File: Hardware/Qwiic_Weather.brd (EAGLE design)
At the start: 25.4 x 25.4 mm, 22 parts, among them J1 Qwiic Right Angle, J3 Qwiic Right Angle, J4 PTH, U3 BME280

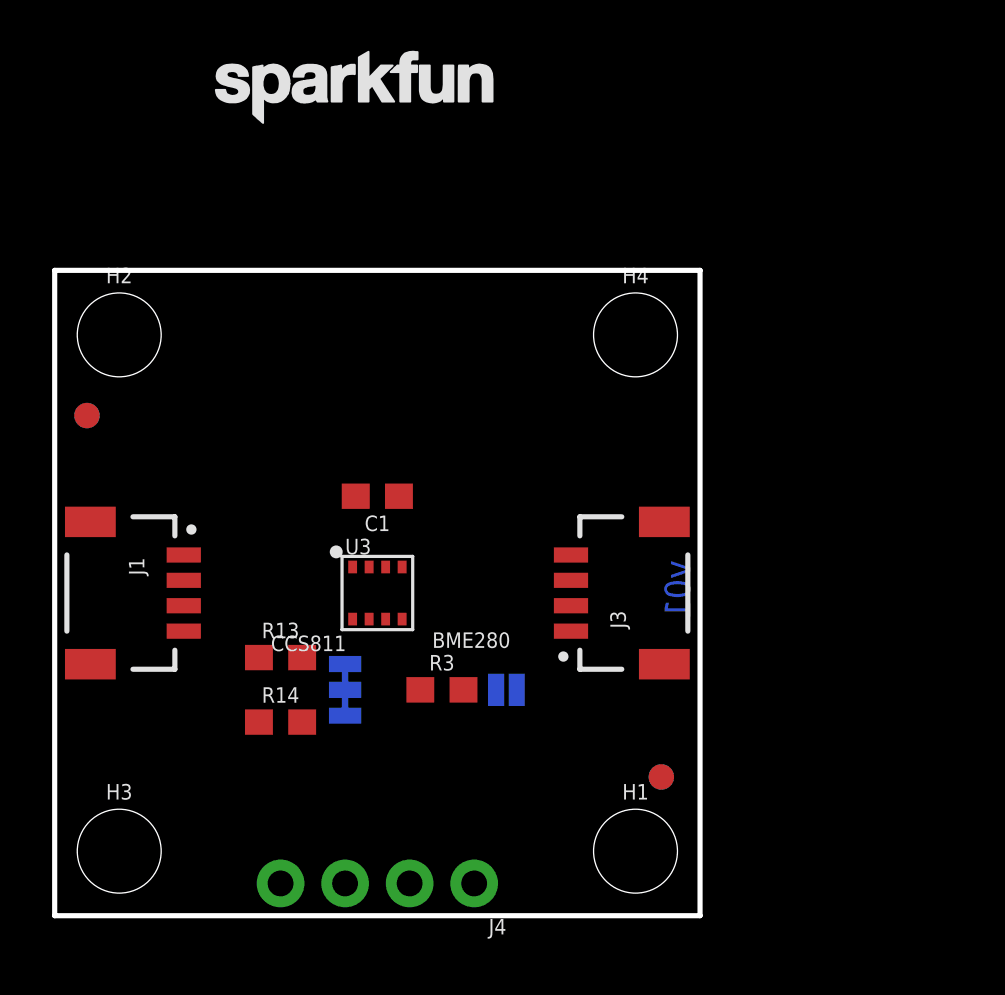
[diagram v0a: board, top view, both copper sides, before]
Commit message: added SPI cabability and some prelim buzzard label work
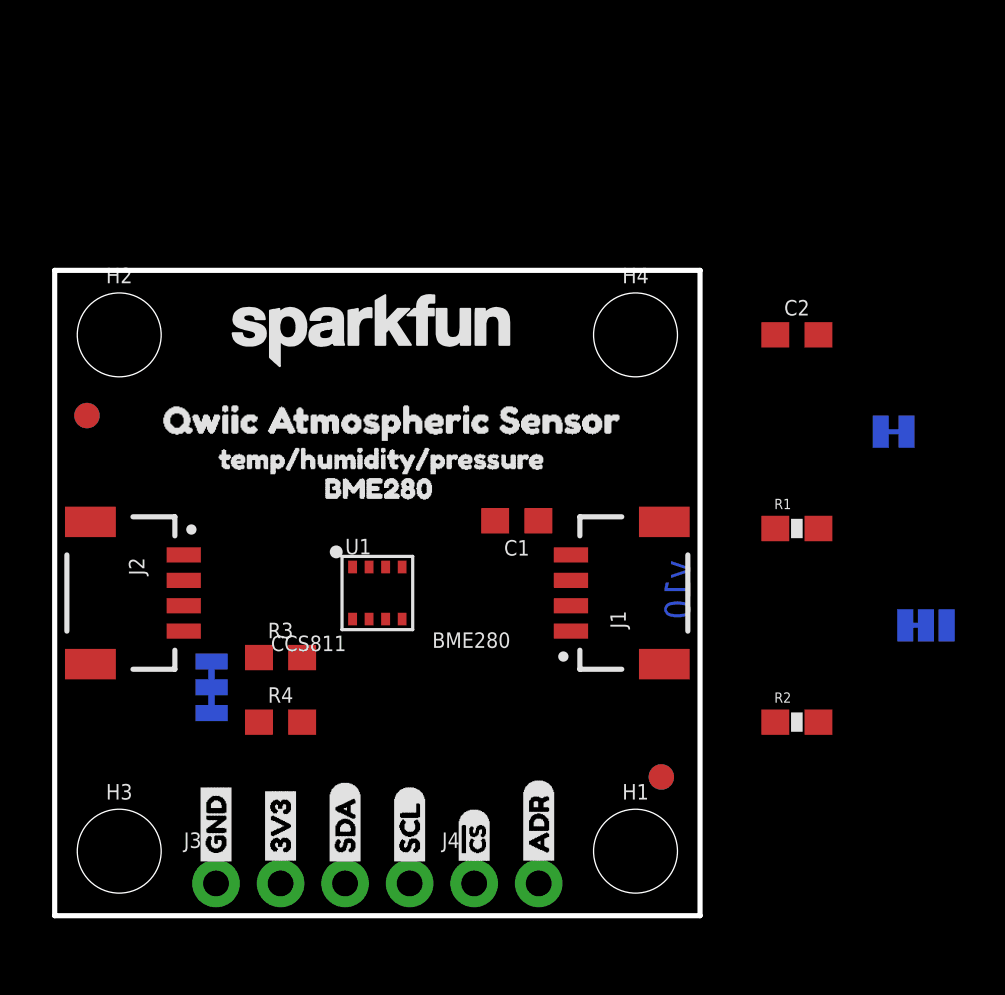
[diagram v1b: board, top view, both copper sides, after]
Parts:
- removed ADDR: ADDR, SparkFun-Jumpers:SMT-JUMPER_2_NO_SILK
- removed JP1: (no value), SparkFun-Jumpers:SMT-JUMPER_3_2-NC_TRACE_SILK
- removed R13: 4.7k, SparkFun-Resistors:0603
- added C2: 0.1uF, SparkFun-Capacitors:0603
- added J2: QWIIC, SparkFun-Connectors:JST04_1MM_RA
- added R1, R2: 4.7K, SparkFun-Resistors:0603-RES
- added SJ1: (no value), SparkFun-Jumpers:SMT-JUMPER_3_2-NC_TRACE_SILK
- added SJ2: EN I2C MODE, SparkFun-Passives:PAD-JUMPER-2-NC_BY_TRACE_YES_SILK
- added SJ3: EN ADR PU, SparkFun-Passives:PAD-JUMPER-3-2OF3_NC_BY_TRACE_YES_SILK_FULL_BOX
- added U$1, U$7: (no value), buzzard_labels:GND0
- added U$10: (no value), buzzard_labels:SDO#ADR8
- added U$11: (no value), buzzard_labels:SCK#SCL7
- added U$12, U$5: (no value), buzzard_labels:#CS4
- added U$13: (no value), buzzard_labels (2):QWIIC_ATMOSPHERIC_SENSOR0
- added U$14: (no value), buzzard_labels (2):TEMP#HUMIDITY#PRESSURE3
- added U$15: (no value), buzzard_labels (2):BME2804
- added U$2, U$8: (no value), buzzard_labels:3V31
- added U$3: (no value), buzzard_labels:SCL3
- added U$4: (no value), buzzard_labels:SDA2
- added U$6: (no value), buzzard_labels:ADR5
- added U$9: (no value), buzzard_labels:SDI#SDA6
- J1: value Qwiic Right Angle -> QWIIC
- J3: value Qwiic Right Angle -> PTH; device SparkFun-Connectors:JST04_1MM_RA -> SparkX:1X04_NO_SILK
- J4: value PTH -> (none); device SparkX:1X04_NO_SILK -> SparkFun-Connectors:1X02_NO_SILK
- R3: value 100k -> 4.7k
- moved LOGO4 25.3 mm to (22.8, 6.50)
- moved J3 18.1 mm to (6.35, 1.27), turned to 0 degrees
- moved J1 15.2 mm to (20.3, 12.7), turned to 90 degrees
- moved LOGO1 9.60 mm to (12.5, 23.0)
- moved R3 6.48 mm to (8.89, 10.2)
- moved C1 5.57 mm to (18.2, 15.5)
- turned J4 to 0 degrees
- renumbered R14 to R4, U3 to U1
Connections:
- removed net SCL: J1.4, J3.4, J4.4, R4.1, U1.4
- removed net SDA: J1.3, J3.3, J4.3, R13.1, U1.3
- new net !CS: J4.1, R1.1, U1.2
- new net N$2: R2.1, SJ3.3
- new net N$6: R1.2, SJ2.1
- new net SCK/SCL: J1.4, J2.4, J3.4, R4.1, U1.4
- new net SDI/SDA: J1.3, J2.3, J3.3, R3.1, U1.3
- net 3.3V: now also C2.1, J2.2, R2.2, SJ1.2, SJ2.2; no longer J4.2, JP1.2, R3.2, U1.2
- net GND: now also C2.2, J2.1, SJ3.1; no longer ADDR.1, J4.1
- net N$4: now also R3.2, SJ1.3; no longer JP1.3, R13.2
- net N$5: now also SJ1.1; no longer JP1.1
- net SDO/ADR: now also J4.2, SJ3.2; no longer ADDR.2, R3.1
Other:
- board text added: "v10"
- board text removed: "v01"

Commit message: Started routing board
About 50% done. Added a power LED, adjusted silk.
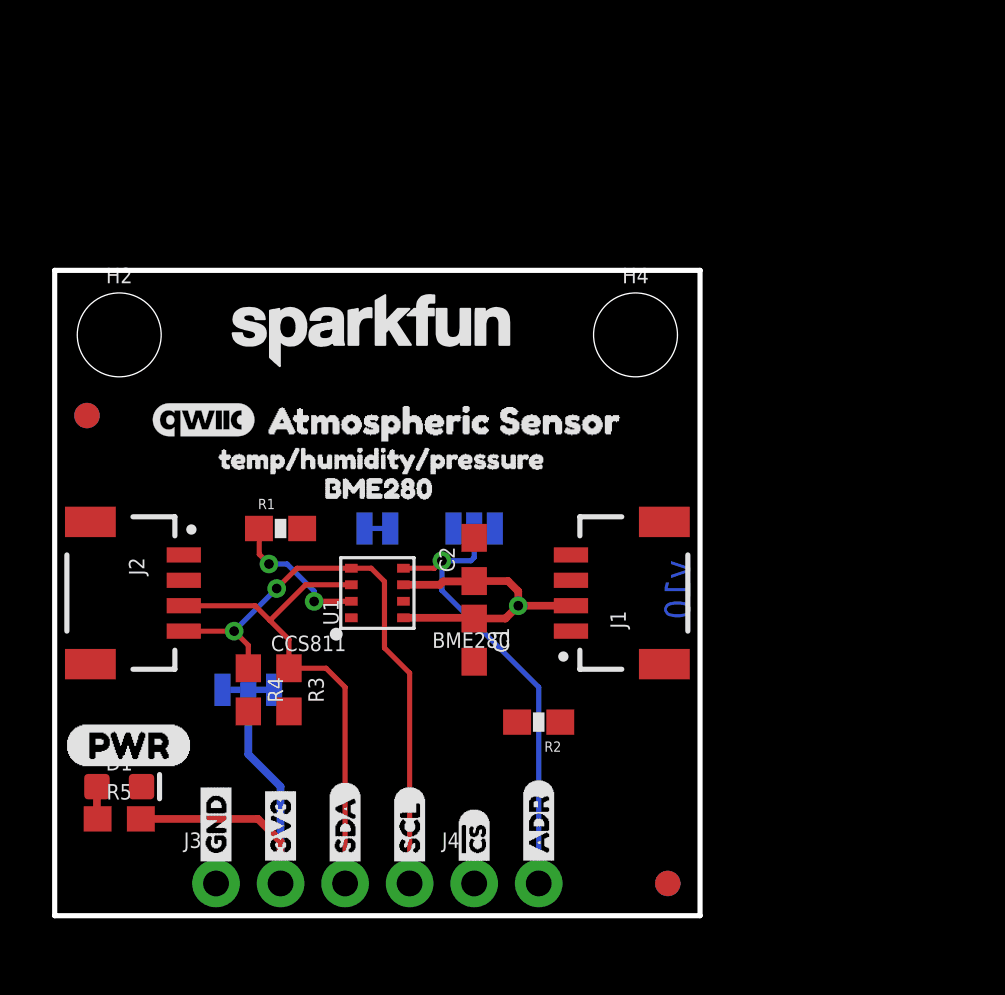
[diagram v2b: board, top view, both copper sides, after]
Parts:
- removed H1, H3: STAND-OFF, SparkFun-Hardware:STAND-OFF
- added D1: RED, SparkFun-LED:LED-0603
- added R5: 1k, SparkFun-Resistors:0603
- added U$16: (no value), SparkFun-Aesthetics:QWIIC_4MM
- added U$17: (no value), buzzard_labels:ATMOSPHERIC_SENSOR0
- U$13: device buzzard_labels (2):QWIIC_ATMOSPHERIC_SENSOR0 -> buzzard_labels (1):PWR0
- moved SJ2 20.7 mm to (12.7, 15.2), turned to 180 degrees
- moved R1 20.3 mm to (8.89, 15.2)
- moved SJ3 18.2 mm to (16.5, 15.2), turned to 180 degrees
- moved C2 15.5 mm to (16.5, 14.0), turned to 90 degrees
- moved U$13 13.1 mm to (0.41, 6.71)
- moved R2 10.2 mm to (19.1, 7.62), turned to 180 degrees
- moved C1 4.99 mm to (16.5, 10.8), turned to 270 degrees
- moved FD2 4.20 mm to (24.1, 1.27)
- moved FD3 4.20 mm to (24.1, 1.27)
- moved R4 1.80 mm to (7.62, 8.89), turned to 270 degrees
- moved SJ1 1.45 mm to (7.62, 8.89), turned to 180 degrees
- moved R3 1.31 mm to (9.22, 8.89), turned to 270 degrees
- turned U1 to 90 degrees
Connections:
- new net N$3: D1.A, R5.1
- net 3.3V: now also R5.2
- net GND: now also D1.C
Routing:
- net 3.3V: track 0.00 -> 27.8 mm, vias 0 -> 1
- net SCK/SCL: track 0.00 -> 23.1 mm, vias 0 -> 2
- net SDI/SDA: track 0.00 -> 19.8 mm
- net SDO/ADR: track 0.00 -> 18.4 mm, vias 0 -> 1
- net !CS: track 0.00 -> 5.65 mm, vias 0 -> 2
- net N$3: track 0.00 -> 1.28 mm

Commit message: Finished Layout
Finished Routing and Added pin and jumper labels.
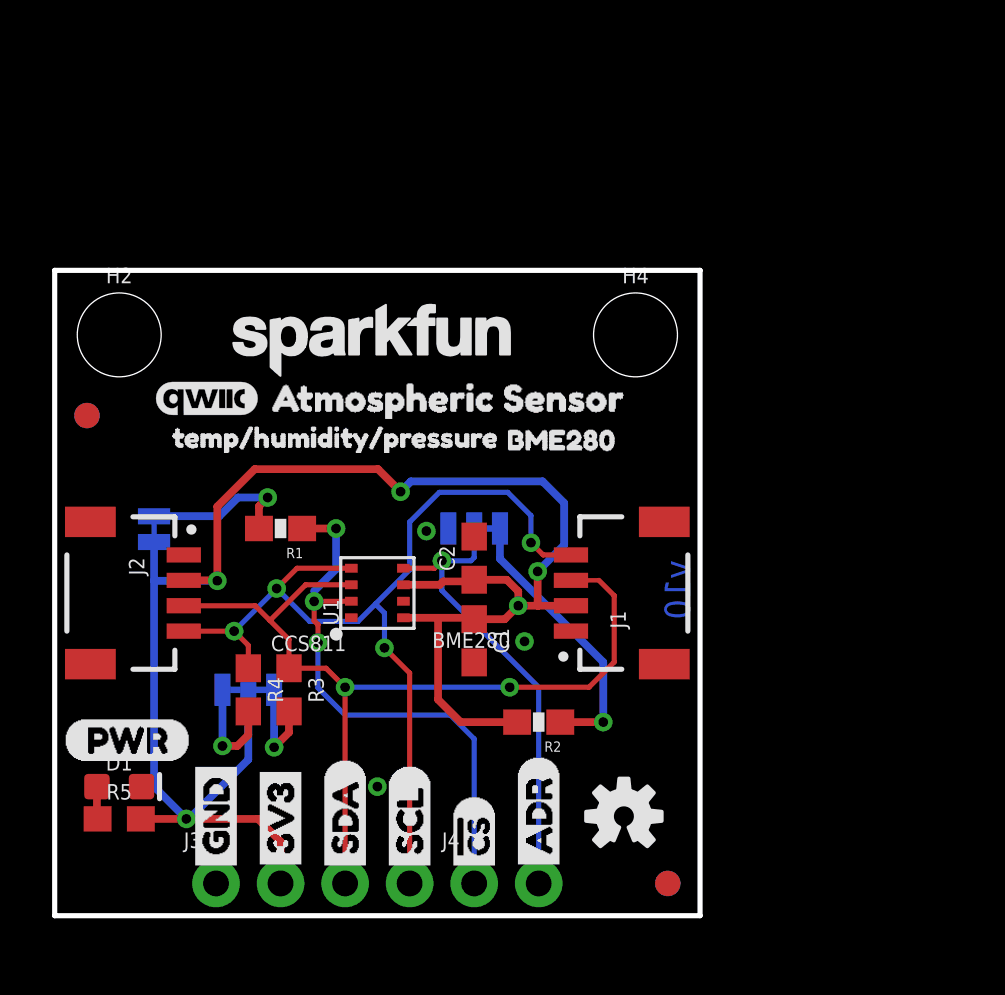
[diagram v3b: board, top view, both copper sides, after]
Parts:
- added U$18: (no value), buzzard_labels:ADR2
- added U$19: (no value), buzzard_labels (2):0X771
- added U$20: (no value), buzzard_labels (2):0X760
- added U$21: (no value), buzzard_labels (3):CS_PU1
- added U$22: (no value), buzzard_labels (3):I2C0
- SJ3: device SparkFun-Passives:PAD-JUMPER-3-2OF3_NC_BY_TRACE_YES_SILK_FULL_BOX -> SparkFun-Jumpers:SMT-JUMPER_3_1-NC_TRACE_NO-SILK
- U$1: device buzzard_labels:GND0 -> buzzard_labels:#CS7
- U$10: device buzzard_labels:SDO#ADR8 -> buzzard_labels:SDO#ADR9
- U$11: device buzzard_labels:SCK#SCL7 -> buzzard_labels:SCK#SCL10
- U$12: device buzzard_labels:#CS4 -> buzzard_labels:#CS7
- U$2: device buzzard_labels:3V31 -> buzzard_labels:3V34
- U$3: device buzzard_labels:SCL3 -> buzzard_labels:ADR8
- U$4: device buzzard_labels:SDA2 -> buzzard_labels:GND3
- U$5: device buzzard_labels:#CS4 -> buzzard_labels:SDA5
- U$6: device buzzard_labels:ADR5 -> buzzard_labels:SCL6
- U$7: device buzzard_labels:GND0 -> buzzard_labels:3V34
- U$8: device buzzard_labels:3V31 -> buzzard_labels:GND3
- U$9: device buzzard_labels:SDI#SDA6 -> buzzard_labels:SDI#SDA11
- moved U$1 10.2 mm to (16.5, 1.30)
- moved SJ2 8.79 mm to (3.91, 15.2), turned to 270 degrees
- moved U$15 7.44 mm to (17.1, 18.7)
- moved LOGO3 6.82 mm to (18.5, 20.8)
- moved U$3 5.09 mm to (19.1, 1.50)
- moved U$4 5.09 mm to (6.35, 1.50)
- moved U$6 5.09 mm to (14.0, 1.50)
- moved U$5 5.08 mm to (11.4, 1.50)
- moved LOGO4 2.62 mm to (22.4, 3.91), flipped to the top
- moved U$7 2.56 mm to (8.89, 1.50)
- moved U$8 2.56 mm to (6.35, 1.50)
- moved U$14 2.01 mm to (3.96, 18.8)
- moved U$17 0.90 mm to (7.65, 20.4)
- moved U$16 0.85 mm to (5.99, 20.3)
- moved LOGO1 0.38 mm to (12.5, 22.7)
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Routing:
- net 3.3V: track 27.8 -> 70.4 mm, vias 1 -> 5
- net !CS: track 5.65 -> 22.2 mm, vias 2 -> 3
- net SDI/SDA: track 19.8 -> 35.4 mm, vias 0 -> 2
- net SCK/SCL: track 23.1 -> 37.8 mm, vias 2 -> 4
- net N$2: track 0.00 -> 11.0 mm, vias 0 -> 1
- net N$6: track 0.00 -> 6.14 mm, vias 0 -> 1
- net N$5: track 0.00 -> 4.33 mm, vias 0 -> 1
- net N$4: track 0.00 -> 3.91 mm, vias 0 -> 1

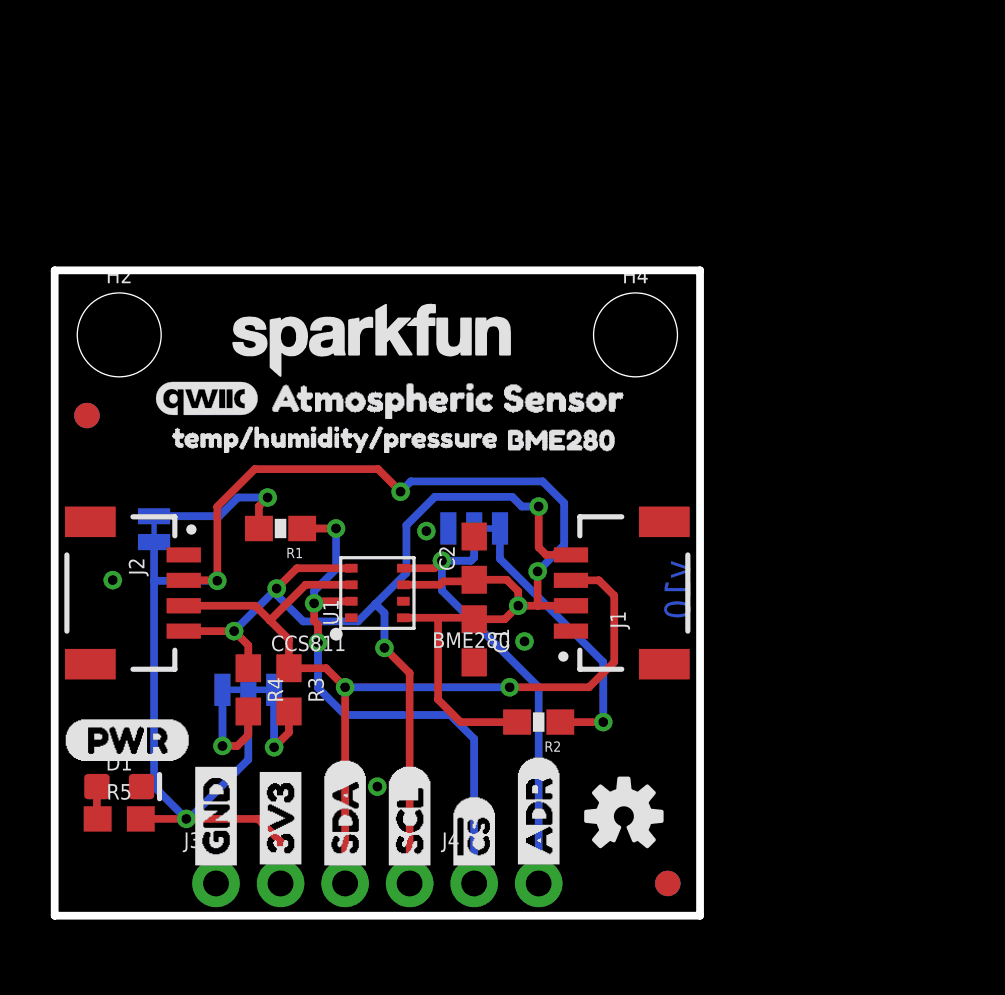
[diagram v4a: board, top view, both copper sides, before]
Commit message: layout and library update work
-updated 4.7K resistors to newest device (no silk under part).
-removed some unncessary vis on 3.3V net, and rerouted.
-nudges some traces and power LED for more efficient routing and better GND flow.
-Moved Jumpers to no silk packages (for consistency)
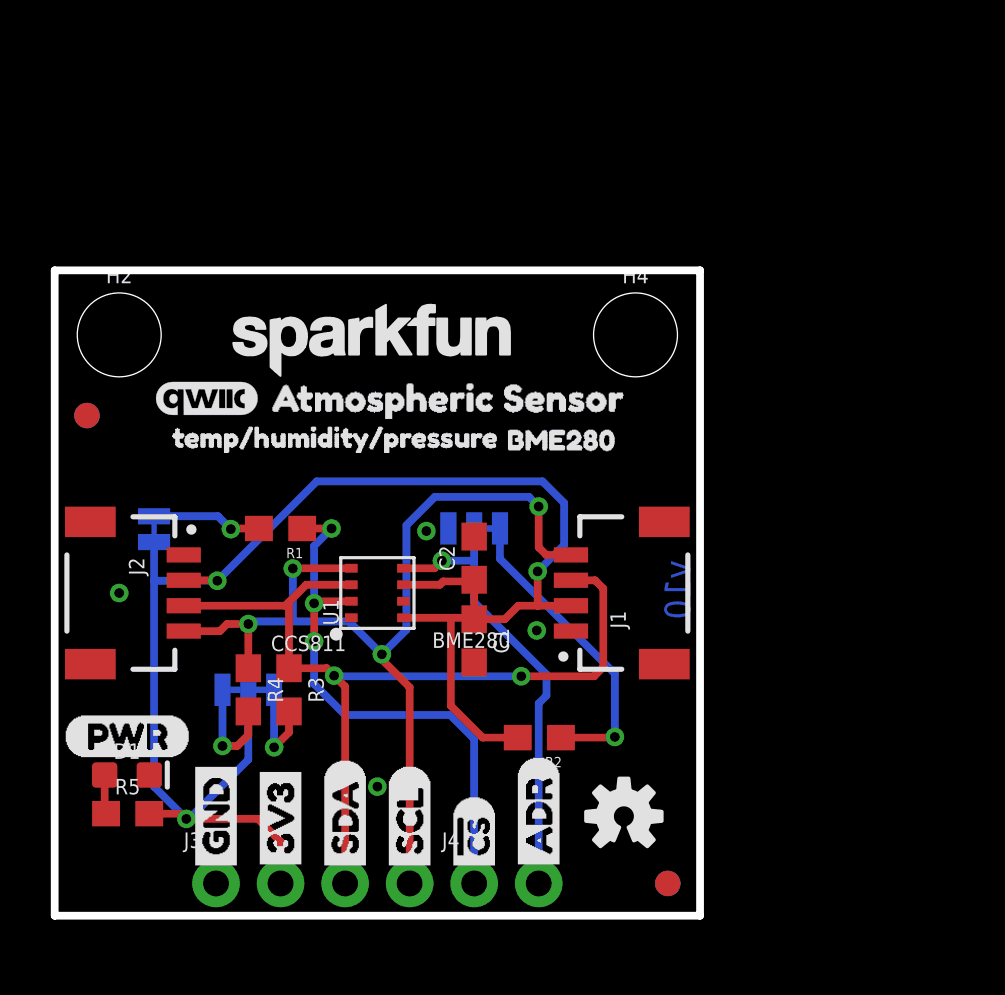
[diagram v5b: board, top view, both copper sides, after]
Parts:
- R1, R2: value 4.7K -> 4.7k; device SparkFun-Resistors:0603-RES -> SparkFun-Resistors:0603
- SJ1: value (none) -> JUMPER-SMT_3_2-NC_TRACE_NO-SILK; device SparkFun-Jumpers:SMT-JUMPER_3_2-NC_TRACE_SILK -> SparkFun-Jumpers:SMT-JUMPER_3_2-NC_TRACE_NO-SILK
- SJ2: device SparkFun-Passives:PAD-JUMPER-2-NC_BY_TRACE_YES_SILK -> SparkFun-Passives:PAD-JUMPER-2-NC_BY_TRACE_NO_SILK
- moved U$22 4.13 mm to (9.65, 10.6)
- moved R2 0.61 mm to (19.1, 7.01)
- moved D1 0.55 mm to (2.84, 5.54)
- moved R5 0.39 mm to (2.87, 4.01)
- moved U$21 0.18 mm to (7.01, 17.1)
- moved U$13 0.15 mm to (0.36, 7.06)
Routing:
- net 3.3V: track 70.4 -> 66.6 mm, vias 5 -> 3
- net N$6: track 6.14 -> 4.35 mm
- net N$2: track 11.0 -> 12.2 mm
